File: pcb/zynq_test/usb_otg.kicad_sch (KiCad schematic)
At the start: 18 parts, among them J1002 USB_A, J1003 Conn_01x02, U1001 TUSB1210-Q1, U1002 DSC1001CI2-026, U1003 AP22816AKBWT

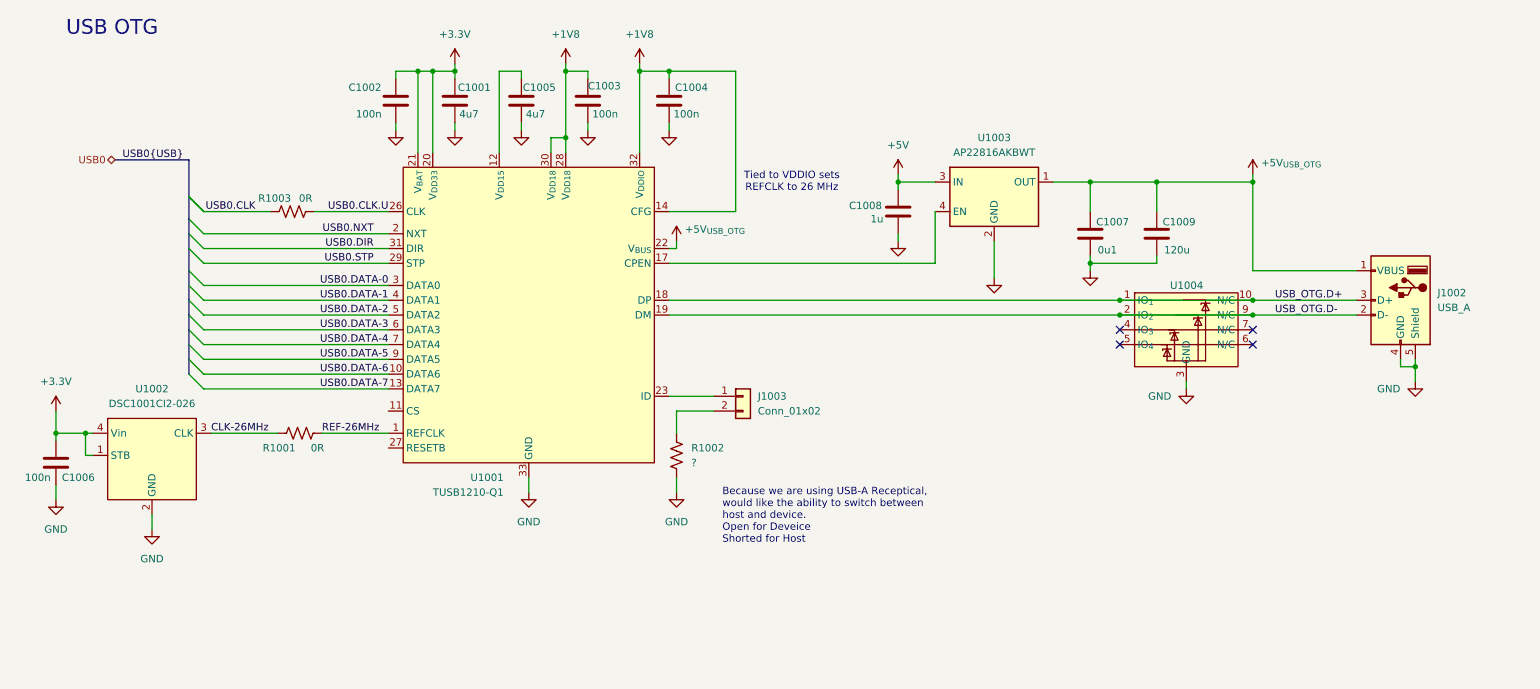
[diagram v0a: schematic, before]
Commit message: Finished HDMI
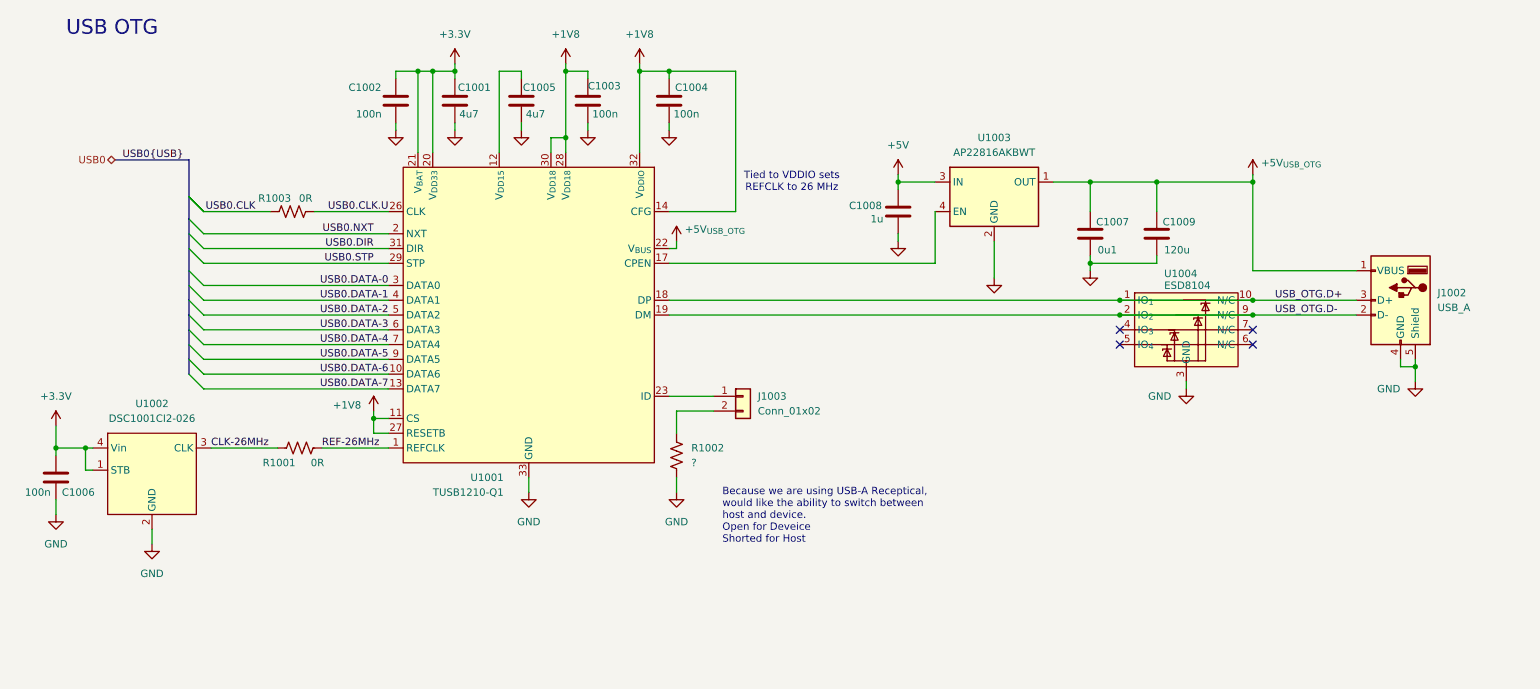
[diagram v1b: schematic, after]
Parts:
- U1001: footprint Package_DFN_QFN:VQFN-32-1EP_5x5mm_P0.5mm_EP3.5x3.5mm_ThermalVias -> Package_DFN_QFN:VQFN-32-1EP_5x5mm_P0.5mm_EP3.5x3.5mm
- U1004: value ~ -> ESD8104
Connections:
- net +1V8: now also U1001.11 (CS), U1001.27 (RESETB)
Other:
- moved on the sheet: C1006, R1001, U1002

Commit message: Connected DDR3, cleaned up some thing
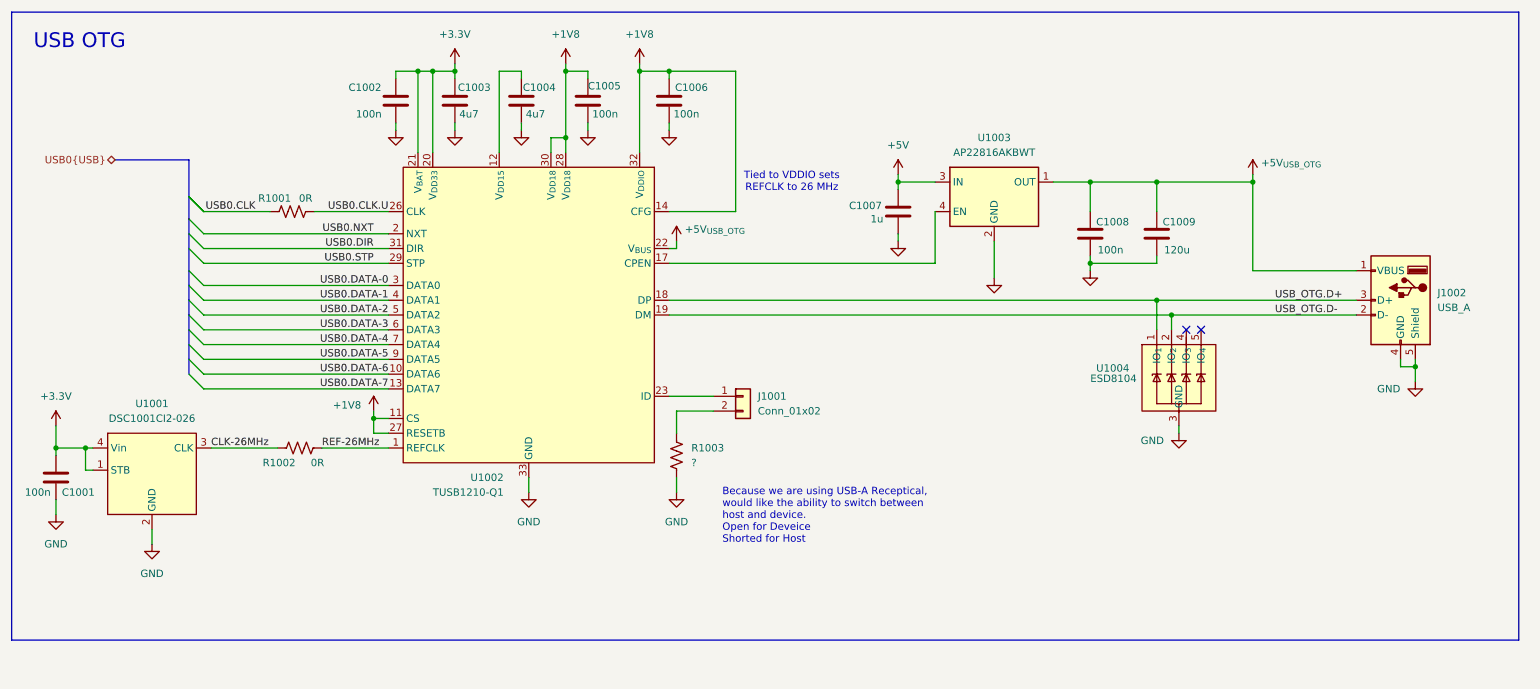
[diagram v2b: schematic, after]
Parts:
- C1008: renamed from C1007; value 0u1 -> 100n
- J1002: footprint (none) -> Connector_USB:USB_A_TE_292303-7_Horizontal
- U1002: renamed from U1001; footprint Package_DFN_QFN:VQFN-32-1EP_5x5mm_P0.5mm_EP3.5x3.5mm -> Package_DFN_QFN:VQFN-32-1EP_5x5mm_P0.5mm_EP3.5x3.5mm_ThermalVias
- renumbered C1006 to C1001, C1001 to C1003, C1005 to C1004, C1003 to C1005, C1004 to C1006, C1008 to C1007, J1003 to J1001, R1003 to R1001, R1001 to R1002, R1002 to R1003, U1002 to U1001
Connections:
- net GND: now also U1004.8 (GND)
- net at U1004.4 (IO_{3}): now also U1004.7 (N/C)
- net at U1004.5 (IO_{4}): now also U1004.6 (N/C)
- no-connect marks 4 -> 2

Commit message: Finished Power Supply
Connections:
- net +3.3V renamed +3V3
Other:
- note removed: "USB OTG"
- title: (none) -> USB OTG
- moved on the sheet: C1001, C1002, C1003, C1004, C1005, C1006, C1007, C1008, C1009, J1001, J1002, R1001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

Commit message: Finished most of the schematic, will start routing soon
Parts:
- U1002: footprint Package_DFN_QFN:VQFN-32-1EP_5x5mm_P0.5mm_EP3.5x3.5mm_ThermalVias -> Package_DFN_QFN:VQFN-32-1EP_5x5mm_P0.5mm_EP3.5x3.5mm
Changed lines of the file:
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@@
 			)
 		)
-		(property "Footprint" "Package_DFN_QFN:VQFN-32-1EP_5x5mm_P0.5mm_EP3.5x3.5mm_ThermalVias"
+		(property "Footprint" "Package_DFN_QFN:VQFN-32-1EP_5x5mm_P0.5mm_EP3.5x3.5mm"
 			(at 101.854 61.214 0)
 			(effects

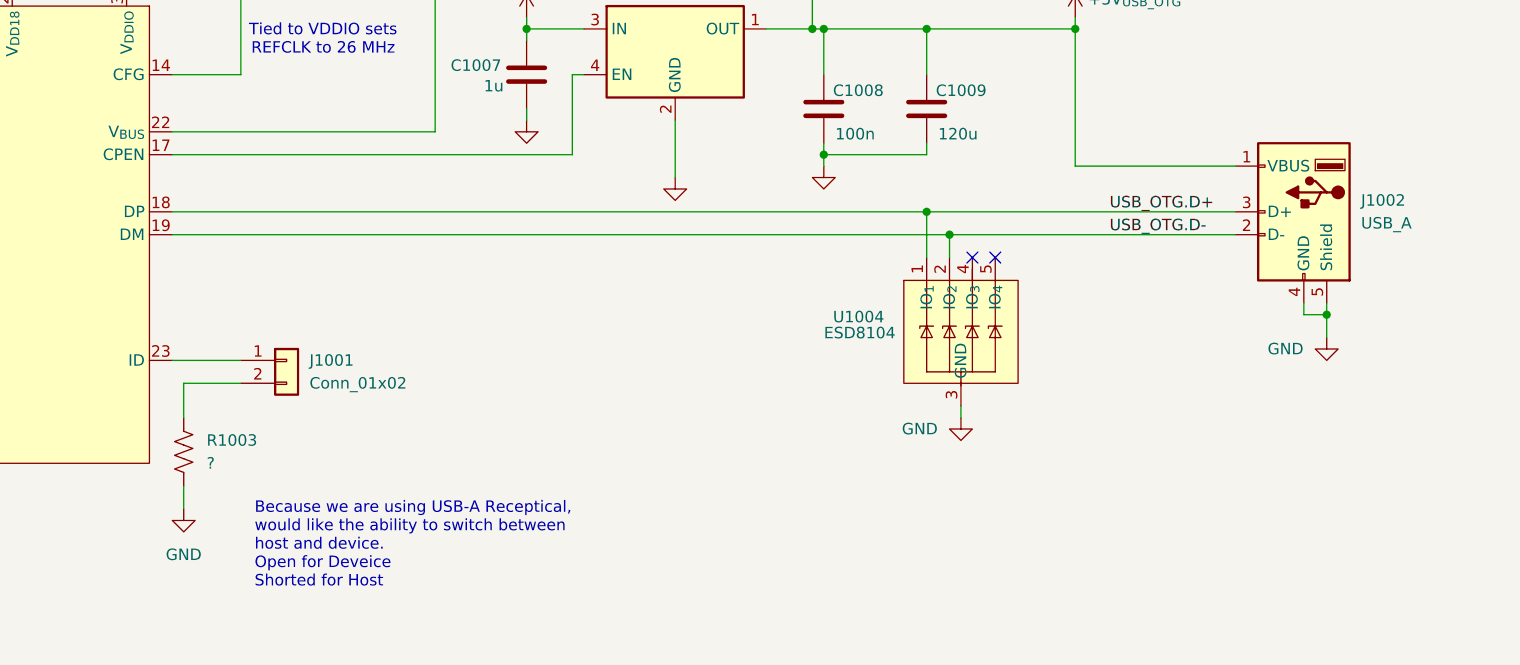
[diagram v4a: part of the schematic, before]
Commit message: finished diff of HDMI
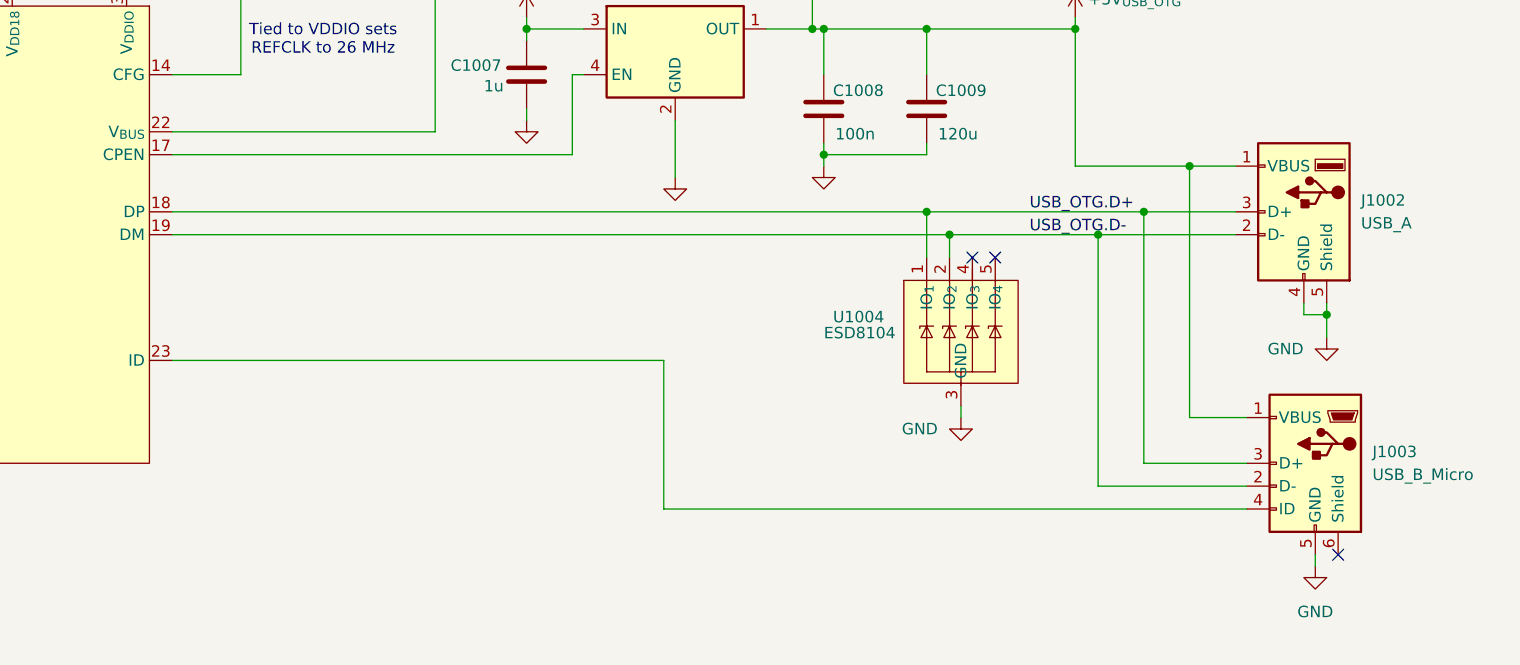
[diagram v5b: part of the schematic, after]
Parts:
- removed J1001: Conn_01x02, symbol Connector_Generic:Conn_01x02
- removed R1003: ?, symbol Device:R_US
- added J1003: USB_B_Micro, Connector_USB:USB_Micro-B_Amphenol_10118193-0001LF_Horizontal, symbol Connector:USB_B_Micro
- R1001: footprint (none) -> Resistor_SMD:R_0402_1005Metric
- U1001: footprint (none) -> other:DSC1001
- U1004: footprint (none) -> Package_DFN_QFN:Diodes_UDFN-10_1.0x2.5mm_P0.5mm
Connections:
- net +5V_{USB_OTG}: now also J1003.1 (VBUS)
- net GND: now also J1003.5 (GND)
- net USB_OTG.D+: now also J1003.3 (D+)
- net USB_OTG.D-: now also J1003.2 (D-)
- net at U1002.23 (ID): now also J1003.4 (ID)
- no-connect marks 2 -> 3
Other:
- note removed: "Because we are using USB-A Receptical, would like the ability to switch between host and device. Open for Deveice Shorted for Host"

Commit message: Almost done with BOM
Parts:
- C1001, C1002, C1003, C1004, C1005, C1006, C1008: footprint (none) -> Capacitor_SMD:C_0402_1005Metric
- C1007: footprint (none) -> Capacitor_SMD:C_0805_2012Metric
- C1009: value 120u -> 100u; footprint (none) -> Capacitor_SMD:C_1210_3225Metric
- R1002: footprint (none) -> Resistor_SMD:R_0402_1005Metric
- renumbered J1002 to J1001, J1003 to J1002
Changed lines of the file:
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@@
 			)
 		)
-		(property "Footprint" ""
+		(property "Footprint" "Resistor_SMD:R_0402_1005Metric"
 			(at 70.104 127.254 90)
 			(effects
@@
 		(on_board yes)
 		(dnp no)
-		(property "Reference" "#PWR01021"
+		(property "Reference" "#PWR01019"
 			(at 233.68 85.09 0)
 			(effects
@@
 			(project "zynq_test"
 				(path "/0637578d-4ce5-4d31-b973-2de977269ea5/f230d79d-5f9c-4b40-9d06-9505b0c2c40c"
-					(reference "#PWR01021")
+					(reference "#PWR01019")
 					(unit 1)
 				)
@@
 			)
 		)
-		(property "Footprint" ""
+		(property "Footprint" "Capacitor_SMD:C_0402_1005Metric"
 			(at 206.7052 95.25 0)
 			(effects
@@
 		(dnp no)
 		(fields_autoplaced yes)
-		(property "Reference" "#PWR01018"
+		(property "Reference" "#PWR01016"
 			(at 189.23 105.41 0)
 			(effects
@@
 			(project "zynq_test"
 				(path "/0637578d-4ce5-4d31-b973-2de977269ea5/f230d79d-5f9c-4b40-9d06-9505b0c2c40c"
-					(reference "#PWR01018")
+					(reference "#PWR01016")
 					(unit 1)
 				)
@@
 			)
 		)
-		(property "Value" "120u"
+		(property "Value" "100u"
 			(at 218.44 94.234 0)
 			(effects
@@
 			)
 		)
-		(property "Footprint" ""
+		(property "Footprint" "Capacitor_SMD:C_1210_3225Metric"
 			(at 218.1352 95.25 0)
 			(effects
@@
 		(dnp no)
 		(fields_autoplaced yes)
-		(property "Reference" "#PWR01016"
+		(property "Reference" "#PWR01014"
 			(at 172.72 85.09 0)
 			(effects
@@
 			(project "zynq_test"
 				(path "/0637578d-4ce5-4d31-b973-2de977269ea5/f230d79d-5f9c-4b40-9d06-9505b0c2c40c"
-					(reference "#PWR01016")
+					(reference "#PWR01014")
 					(unit 1)
 				)
@@
 		(dnp no)
 		(fields_autoplaced yes)
-		(property "Reference" "#PWR01019"
+		(property "Reference" "#PWR01017"
 			(at 205.74 104.14 0)
 			(effects
@@
 			(project "zynq_test"
 				(path "/0637578d-4ce5-4d31-b973-2de977269ea5/f230d79d-5f9c-4b40-9d06-9505b0c2c40c"
-					(reference "#PWR01019")
+					(reference "#PWR01017")
 					(unit 1)
 				)
@@
 			)
 		)
-		(property "Footprint" ""
+		(property "Footprint" "Capacitor_SMD:C_0402_1005Metric"
 			(at 28.9052 137.16 0)
 			(effects
@@
 		(on_board yes)
 		(dnp no)
-		(property "Reference" "#PWR01022"
+		(property "Reference" "#PWR01021"
 			(at 261.62 123.19 0)
 			(effects
@@
 			(project "zynq_test"
 				(path "/0637578d-4ce5-4d31-b973-2de977269ea5/f230d79d-5f9c-4b40-9d06-9505b0c2c40c"
-					(reference "#PWR01022")
+					(reference "#PWR01021")
 					(unit 1)
 				)
@@
 			)
 		)
-		(property "Footprint" ""
+		(property "Footprint" "Capacitor_SMD:C_0402_1005Metric"
 			(at 108.9152 72.39 0)
 			(effects
@@
 			)
 		)
-		(property "Footprint" ""
+		(property "Footprint" "Capacitor_SMD:C_0402_1005Metric"
 			(at 134.3152 72.39 0)
 			(effects
@@
 			)
 		)
-		(property "Footprint" ""
+		(property "Footprint" "Capacitor_SMD:C_0805_2012Metric"
 			(at 171.7548 91.44 0)
 			(effects
@@
 		(dnp no)
 		(fields_autoplaced yes)
-		(property "Reference" "J1002"
+		(property "Reference" "J1001"
 			(at 265.43 101.5999 0)
 			(effects
@@
 			(project "zynq_test"
 				(path "/0637578d-4ce5-4d31-b973-2de977269ea5/f230d79d-5f9c-4b40-9d06-9505b0c2c40c"
-					(reference "J1002")
+					(reference "J1001")
 					(unit 1)
 				)
@@
 		(dnp no)
 		(fields_autoplaced yes)
-		(property "Reference" "#PWR01017"
+		(property "Reference" "#PWR01015"
 			(at 172.72 99.06 0)
 			(effects
@@
 			(project "zynq_test"
 				(path "/0637578d-4ce5-4d31-b973-2de977269ea5/f230d79d-5f9c-4b40-9d06-9505b0c2c40c"
-					(reference "#PWR01017")
+					(reference "#PWR01015")
 					(unit 1)
 				)
@@
 		(dnp no)
 		(fields_autoplaced yes)
-		(property "Reference" "#PWR01014"
+		(property "Reference" "#PWR01020"
 			(at 260.35 148.59 0)
 			(effects
@@
 			(project "zynq_test"
 				(path "/0637578d-4ce5-4d31-b973-2de977269ea5/f230d79d-5f9c-4b40-9d06-9505b0c2c40c"
-					(reference "#PWR01014")
+					(reference "#PWR01020")
 					(unit 1)
 				)
@@
 			)
 		)
-		(property "Footprint" ""
+		(property "Footprint" "Capacitor_SMD:C_0402_1005Metric"
 			(at 120.3452 72.39 0)
 			(effects
@@
 		(dnp no)
 		(fields_autoplaced yes)
-		(property "Reference" "J1003"
+		(property "Reference" "J1002"
 			(at 266.7 129.5399 0)
 			(effects
@@
 			(project "zynq_test"
 				(path "/0637578d-4ce5-4d31-b973-2de977269ea5/f230d79d-5f9c-4b40-9d06-9505b0c2c40c"
-					(reference "J1003")
+					(reference "J1002")
 					(unit 1)
 				)
@@
 		(on_board yes)
 		(dnp no)
-		(property "Reference" "#PWR01020"
+		(property "Reference" "#PWR01018"
 			(at 220.98 132.08 0)
 			(effects
@@
 			(project "zynq_test"
 				(path "/0637578d-4ce5-4d31-b973-2de977269ea5/f230d79d-5f9c-4b40-9d06-9505b0c2c40c"
-					(reference "#PWR01020")
+					(reference "#PWR01018")
 					(unit 1)
 				)
@@
 			)
 		)
-		(property "Footprint" ""
+		(property "Footprint" "Capacitor_SMD:C_0402_1005Metric"
 			(at 87.3252 72.39 0)
 			(effects
@@
 			)
 		)
-		(property "Footprint" ""
+		(property "Footprint" "Capacitor_SMD:C_0402_1005Metric"
 			(at 97.4852 72.39 0)
 			(effects

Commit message: Version sent to JLCPCB
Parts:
- C1001, C1002, C1005, C1006, C1008: JLCPCB Part# (none) -> C1525; PART_NUMBER (none) -> CL05B104KO5NNNC
- C1003, C1004: JLCPCB Part# (none) -> C23733; PART_NUMBER (none) -> CL05A475MP5NRNC
- C1007: JLCPCB Part# (none) -> C28323; PART_NUMBER (none) -> CL21B105KBFNNNE
- C1009: JLCPCB Part# (none) -> C23742; PART_NUMBER (none) -> CL32A107MPVNNNE
- J1001: JLCPCB Part# (none) -> C591560; PART_NUMBER (none) -> 292303-7
- J1002: JLCPCB Part# (none) -> C132562; PART_NUMBER (none) -> 10118193-0001LF
- R1001, R1002: JLCPCB Part# (none) -> C242160; PART_NUMBER (none) -> ERJ2GE0R00X
- U1001: JLCPCB Part# (none) -> C611426; PART_NUMBER (none) -> DSC1001CI5-026.0000
- U1002: JLCPCB Part# (none) -> C2652869; PART_NUMBER (none) -> TUSB1210BRHBR
- U1003: JLCPCB Part# (none) -> C5157836; PART_NUMBER (none) -> AP22816AKBWT-7
- U1004: JLCPCB Part# (none) -> C94394; PART_NUMBER (none) -> ESD8104MUTAG
